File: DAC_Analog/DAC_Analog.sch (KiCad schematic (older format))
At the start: 0 parts

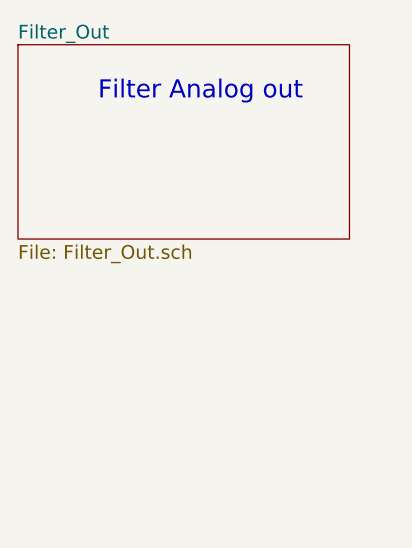
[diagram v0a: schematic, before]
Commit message: update DAC schematic
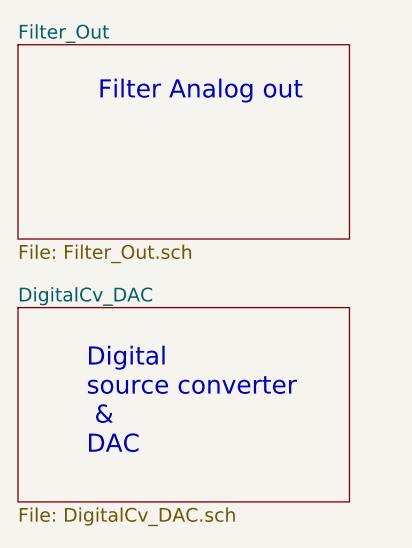
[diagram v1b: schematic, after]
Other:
- note added: "Digital \nsource converter\n &\nDAC"
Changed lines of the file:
@@
 $Descr A4 11693 8268
 encoding utf-8
-Sheet 1 2
+Sheet 1 3
 Title ""
 Date ""
@@
 Text Notes 8600 2350 0    79   ~ 0
 Filter Analog out
+$Sheet
+S 8250 3250 1450 850
+U 599B5101
+F0 "DigitalCv_DAC" 60
+F1 "DigitalCv_DAC.sch" 60
+$EndSheet
+Text Notes 8550 3900 0    79   ~ 0
+Digital \nsource converter\n &\nDAC
 $EndSCHEMATC
